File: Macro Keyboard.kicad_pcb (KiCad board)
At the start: 2 copper layers, 113 parts, among them J2901 FPC 1x24, Q2901 Q_PJFET_GDS, SW1001 KH-PS1611-54, SW1101 KH-PS1611-54, SW1201 KH-PS1611-54, SW1301 KH-PS1611-54, SW1401 KH-PS1611-54, SW1501 KH-PS1611-54, SW2801 SWITCH TACTILE SPST-NO 50MA 1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, SW601 KH-PS1611-54, SW701 KH-PS1611-54, SW801 KH-PS1611-54, SW901 KH-PS1611-54, U2701 PCA9745BTWJ, U2801 Pico-JER, U301 VEML7700, U401 PI4ULS5V201TAEX

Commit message: Checkpoint
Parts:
- C1701, C1801, C1901, C2001, C2101, C2201, C2301, C2401, C2501, C2601: moved to B.Cu
- moved C1701 25.3 mm to (26.5, 65.3), turned to 270 degrees
- moved D1701 22.2 mm to (26.4, 65.5), turned to 180 degrees
- moved C601 16.2 mm to (22.6, 46.6), turned to 270 degrees
- moved R602 14.7 mm to (29.0, 46.6), turned to 270 degrees
- moved R601 14.2 mm to (25.9, 46.6), turned to 90 degrees
- moved C2201 7.00 mm to (189.6, 65.3), turned to 90 degrees
- moved C1901 7.00 mm to (192.6, 28.4), turned to 90 degrees
- moved C2101 7.00 mm to (233.6, 64.4), turned to 90 degrees
- moved C2301 7.00 mm to (140.4, 67.0), turned to 90 degrees
- moved C2401 7.00 mm to (140.0, 101.2), turned to 90 degrees
- moved C2501 7.00 mm to (187.6, 101.4), turned to 90 degrees
- moved C1801 7.00 mm to (140.6, 28.1), turned to 90 degrees
- moved C2001 7.00 mm to (235.0, 26.7), turned to 90 degrees
- moved C2601 7.00 mm to (232.3, 101.8), turned to 90 degrees
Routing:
- net GND: track 0.00 -> 4.70 mm, vias 0 -> 1
- net +5V: track 0.00 -> 4.35 mm, vias 0 -> 1
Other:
- net class 1-wire added: clearance 0.4, trace_width 0.2, via_dia 0.8, via_drill 0.4
- net class Diff Pair added: clearance 0.2, trace_width 0.8125, via_dia 0.8, via_drill 0.4
- net class Power added: clearance 0.2, trace_width 0.5, via_dia 0.8, via_drill 0.4

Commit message: Switch NeoPixel to SK6812MINI-E
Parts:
- D1701, D1801, D1901, D2001, D2101, D2201, D2301, D2401, D2501, D2601: value WS2812B -> SK6812MINI-E; footprint LED_SMD:LED_WS2812B_PLCC4_5.0x5.0mm_P3.2mm -> Macro Keyboard:MX_SK6812MINI-E
- moved D2401 218.5 mm to (358.6, 104.6)
- moved D2601 216.3 mm to (443.5, 54.2)
- moved D2501 214.4 mm to (401.0, 79.4)
- moved D2201 211.6 mm to (401.0, 54.2)
- moved D2301 186.5 mm to (316.1, 129.8)
- moved D1801 182.8 mm to (316.1, 79.4)
- moved D1901 167.9 mm to (358.6, 54.2)
- moved D2101 125.8 mm to (358.6, 79.4)
- moved D2001 112.4 mm to (316.1, 104.6)
- moved D1701 6.90 mm to (26.4, 58.6), turned to 0 degrees
- moved C1701 6.33 mm to (20.4, 63.7), turned to 90 degrees
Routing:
- net GND: track 4.70 -> 0.00 mm, vias 1 -> 0
- net +5V: track 4.35 -> 0.00 mm, vias 1 -> 0
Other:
- board outline added: 3.6 x 3.3 mm

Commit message: design checkpoint
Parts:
- added C3001: 1 uF 10% 10V, Capacitor_SMD:C_0805_2012Metric_Pad1.18x1.45mm_HandSolder, F.Cu at (126.2, 92.7)
- added C3002: 1 uF 10% 10V, Capacitor_SMD:C_0805_2012Metric_Pad1.18x1.45mm_HandSolder, F.Cu at (126.2, 95.7)
- added C3003: 1 uF 10% 10V, Capacitor_SMD:C_0805_2012Metric_Pad1.18x1.45mm_HandSolder, F.Cu at (131.0, 92.7)
- added R3001: 4.7k 5%, Resistor_SMD:R_0805_2012Metric_Pad1.20x1.40mm_HandSolder, F.Cu at (126.2, 98.7)
- added R3002: 47k 5%, Resistor_SMD:R_0805_2012Metric_Pad1.20x1.40mm_HandSolder, F.Cu at (131.0, 95.7)
- added R3003: 4.7k 5%, Resistor_SMD:R_0805_2012Metric_Pad1.20x1.40mm_HandSolder, F.Cu at (135.8, 92.7)
- added R3004: 47k 5%, Resistor_SMD:R_0805_2012Metric_Pad1.20x1.40mm_HandSolder, F.Cu at (126.2, 101.6)
- added R3005: 150 5%, Resistor_SMD:R_0805_2012Metric_Pad1.20x1.40mm_HandSolder, F.Cu at (130.9, 98.7)
- added R3006: 2.7k 5%, Resistor_SMD:R_0805_2012Metric_Pad1.20x1.40mm_HandSolder, F.Cu at (135.7, 95.7)
- added R3007: 4.7k 5%, Resistor_SMD:R_0805_2012Metric_Pad1.20x1.40mm_HandSolder, F.Cu at (126.2, 104.6)
- added R3008: 68 5%, Resistor_SMD:R_0805_2012Metric_Pad1.20x1.40mm_HandSolder, F.Cu at (130.9, 101.6)
- added R3009: 68 5%, Resistor_SMD:R_0805_2012Metric_Pad1.20x1.40mm_HandSolder, F.Cu at (135.7, 98.6)
- added S3001: ENCODER-RGB-SWITCH, Macro Keyboard:ENCODER_LED_3, F.Cu at (117.0, 99.0)
- C2901, C2902, C2903, C2904, C2905, C2906, C2907, C2908, C2909, D2901, D2902, D2903, L2901, Q2901, R2901, R2902, U2801: moved to B.Cu
- moved C901 159.9 mm to (95.2, 81.6)
- moved R901 159.9 mm to (95.1, 84.6)
- moved R902 159.9 mm to (99.9, 81.6)
- moved C1001 152.2 mm to (96.5, 102.1)
- moved R1001 152.2 mm to (96.5, 105.0)
- moved R1002 152.2 mm to (101.3, 102.0)
- moved C1501 148.8 mm to (96.6, 120.7)
- moved R1501 148.8 mm to (96.6, 123.6)
- moved R1502 148.8 mm to (101.4, 120.6)
- moved C2001 147.1 mm to (96.4, 75.8)
- moved SW901 143.1 mm to (98.0, 80.0)
- moved C2601 140.6 mm to (92.2, 112.6)
- moved C2101 140.4 mm to (96.3, 93.7)
- moved SW1001 137.3 mm to (98.0, 99.0)
- moved SW1501 135.2 mm to (98.0, 118.0)
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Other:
- board size 3.6 x 3.3 mm -> 90.3 x 113.3 mm

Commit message: Starting routing
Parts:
- added DS**: e-paper_E2154FS091, Macro Keyboard:e-paper_E2154FS091, F.Cu at (55.4, 33.8)
- added REF**: MountingHole_M3_StandoffSMD, TMPPCB_R2:MountingHole_M3_StandoffSMD, F.Cu at (143.5, 35.5)
- added REF**: MountingHole_M3_StandoffSMD, TMPPCB_R2:MountingHole_M3_StandoffSMD, F.Cu at (56.4, 36.2)
- C1001, C1101, C1201, C1301, C1401, C1501, C2801, C2802, C701, C801, C901, R1001, R1002, R1101, R1102, R1201, R1202, R1301, R1302, R1401, R1402, R1501, R1502, R2801, R701, R702, R801, R802, R901, R902, SW2801: moved to B.Cu
- D2101, D2201, D2301: footprint Macro Keyboard:MX_SK6812MINI-E -> Macro Keyboard:MX_SK6812MINI-E_REV
- moved D2601 351.2 mm to (98.1, 118.1), turned to 180 degrees
- moved D2201 325.1 mm to (79.0, 99.0), turned to 180 degrees
- moved D2501 324.3 mm to (79.0, 118.1), turned to 180 degrees
- moved D2401 298.9 mm to (60.0, 118.1), turned to 180 degrees
- moved D1901 280.7 mm to (79.0, 80.0), turned to 180 degrees
- moved D2101 261.2 mm to (98.1, 99.0), turned to 180 degrees
- moved D2301 257.9 mm to (60.0, 99.0), turned to 180 degrees
- moved D1801 256.1 mm to (60.0, 80.0), turned to 180 degrees
- moved D2001 219.4 mm to (98.1, 80.0), turned to 180 degrees
- moved U2801 134.8 mm to (78.8, 57.7), turned to 270 degrees
- moved R2701 112.8 mm to (130.0, 57.3)
- moved R2702 112.8 mm to (134.8, 51.4)
- moved R2703 112.8 mm to (130.0, 54.4)
- moved R2704 112.8 mm to (134.8, 54.4)
- moved R2705 112.8 mm to (130.0, 60.3)
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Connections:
- J2901 pad 1: (no net) -> Net-(J2901-Pad1)
- J2901 pad 19: (no net) -> Net-(J2901-Pad19)
- J2901 pad 4: (no net) -> Net-(J2901-Pad4)
- J2901 pad 6: (no net) -> Net-(J2901-Pad6)
- J2901 pad 7: (no net) -> Net-(J2901-Pad7)
- R3005 pad 1: (no net) -> /Rotary Encoder 2/REnc_LED_R_5V
- R3008 pad 1: (no net) -> /Rotary Encoder 2/REnc_LED_G_5V
- R3009 pad 1: (no net) -> /Rotary Encoder 2/REnc_LED_B_5V
- U2701 pad 11: (no net) -> Net-(U2701-Pad11)
- U2701 pad 12: (no net) -> Net-(U2701-Pad12)
- U2701 pad 13: (no net) -> Net-(U2701-Pad13)
- U2701 pad 14: (no net) -> Net-(U2701-Pad14)
- U2701 pad 15: (no net) -> Net-(U2701-Pad15)
- U2701 pad 16: (no net) -> Net-(U2701-Pad16)
- U2701 pad 17: (no net) -> Net-(U2701-Pad17)
- U2701 pad 18: (no net) -> Net-(U2701-Pad18)
- U2701 pad 20: (no net) -> Net-(U2701-Pad20)
- U2701 pad 21: (no net) -> Net-(U2701-Pad21)
- U2701 pad 22: (no net) -> Net-(U2701-Pad22)
- U2701 pad 23: (no net) -> Net-(U2701-Pad23)
- U2701 pad 9: (no net) -> Net-(U2701-Pad9)
- U2801 pad 31: (no net) -> /Pico/GPIO_26_ADC0
- U2801 pad 32: (no net) -> /Pico/GPIO_27_ADC1
- U2801 pad 34: (no net) -> /Pico/GPIO_28_ADC2
- U2801 pad 37: (no net) -> Net-(U2801-Pad37)
- U2801 pad 39: (no net) -> Net-(U2801-Pad39)
- U2801 pad 41: (no net) -> Net-(U2801-Pad41)
- U2801 pad 43: (no net) -> Net-(U2801-Pad43)
- U2801 pad 44: (no net) -> Net-(U2801-Pad44)
- U2801 pad 45: (no net) -> Net-(U2801-Pad45)
- U2801 pad 46: (no net) -> Net-(U2801-Pad46)
- U2801 pad 47: (no net) -> Net-(U2801-Pad47)
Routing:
- net /Pico/GPIO_07: track 0.00 -> 74.0 mm, vias 0 -> 2
- net /Pico/GPIO_04: track 0.00 -> 45.8 mm, vias 0 -> 2
- net /Pico/GPIO_02: track 0.00 -> 38.7 mm, vias 0 -> 2
- net /Pico/GPIO_03: track 0.00 -> 38.6 mm, vias 0 -> 2
- net /LED 10/Neo LED 05/D_IN: track 0.00 -> 26.1 mm
- net /LED 10/Neo LED 08/D_IN: track 0.00 -> 21.7 mm
- net +5V: track 0.00 -> 20.0 mm
- net /LED 10/Neo LED 04/D_IN: track 0.00 -> 14.5 mm
- net /LED 10/Neo LED 09/D_IN: track 0.00 -> 14.5 mm
- net /LED 10/Neo LED 07/D_IN: track 0.00 -> 14.5 mm
- net /LED 10/Neo LED 06/D_IN: track 0.00 -> 14.5 mm
- net /LED 10/Neo LED 03/D_IN: track 0.00 -> 14.5 mm
- net /10 Group Switch/Switch 5/SW_RDIV: track 0.00 -> 8.77 mm
- net /10 Group Switch/Switch 4/SW_RDIV: track 0.00 -> 8.77 mm
- net /10 Group Switch/Switch 10/SW_RDIV: track 0.00 -> 8.77 mm
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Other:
- board size 90.3 x 113.3 mm -> 101.6 x 123.4 mm

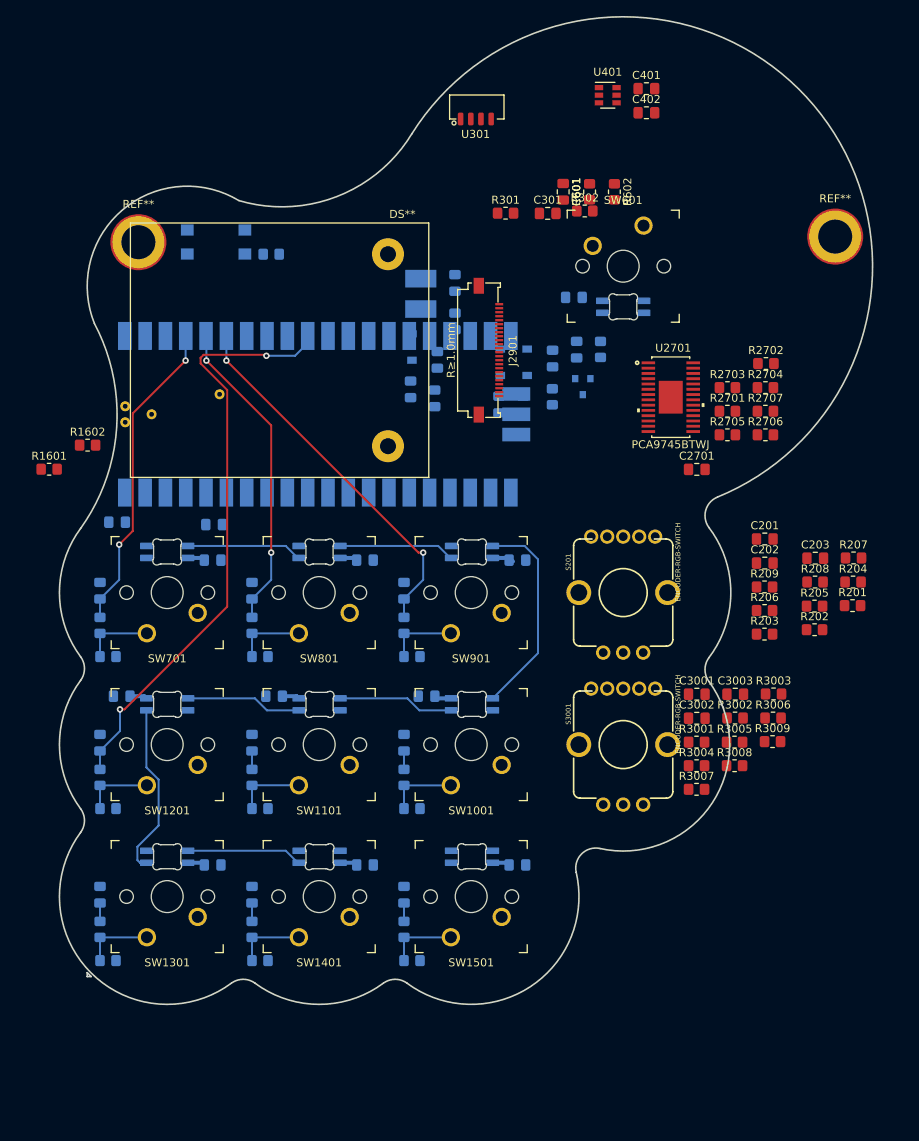
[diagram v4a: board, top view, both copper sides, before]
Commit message: Layout completed. Design check passes.
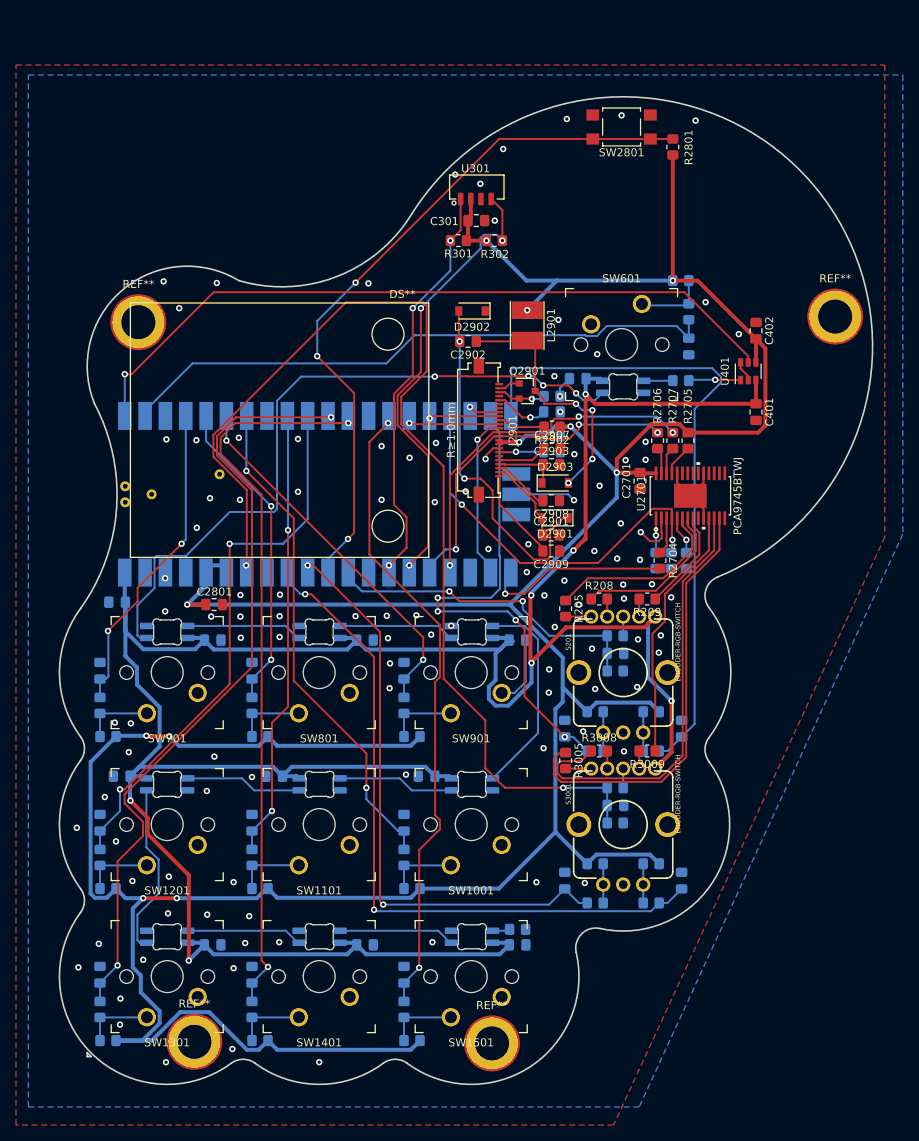
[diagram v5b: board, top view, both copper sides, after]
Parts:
- removed the REF** at (143.5, 35.5)
- removed the REF** at (56.4, 36.2)
- added REF**: MountingHole_M3_StandoffSMD, TMPPCB_R2:MountingHole_M3_StandoffSMD, F.Cu at (100.6, 136.3)
- added REF**: MountingHole_M3_StandoffSMD, TMPPCB_R2:MountingHole_M3_StandoffSMD, F.Cu at (63.4, 136.2)
- added REF**: MountingHole_M3_StandoffSMD, TMPPCB_R2:MountingHole_M3_StandoffSMD, F.Cu at (143.5, 45.5)
- added REF**: MountingHole_M3_StandoffSMD, TMPPCB_R2:MountingHole_M3_StandoffSMD, F.Cu at (56.4, 46.2)
- C201, C202, C203, C3001, C3002, C3003, C601, R1601, R1602, R201, R202, R203, R204, R206, R207, R2701, R2702, R2703, R3001, R3002, R3003, R3004, R3006, R3007, R601, R602: moved to B.Cu
- C2801, C2901, C2902, C2903, C2907, C2908, C2909, D2901, D2902, D2903, L2901, Q2901, R2801, R2902, SW2801: moved to F.Cu
- moved R1602 81.0 mm to (103.8, 122.1), turned to 180 degrees
- moved R1601 79.7 mm to (124.2, 53.5)
- moved SW2801 52.7 mm to (116.8, 21.8), turned to 180 degrees
- moved R2801 52.0 mm to (123.2, 24.3), turned to 90 degrees
- moved C401 42.7 mm to (133.6, 57.4), turned to 270 degrees
- moved U401 38.7 mm to (132.6, 52.3), turned to 90 degrees
- moved R201 36.9 mm to (113.5, 99.8)
- moved C201 34.4 mm to (109.7, 97.0), turned to 90 degrees
- moved R207 33.0 mm to (116.0, 89.8), turned to 180 degrees
- moved R205 31.1 mm to (109.8, 82.0), turned to 270 degrees
- moved C402 30.5 mm to (133.6, 47.3), turned to 270 degrees
- moved R3003 30.3 mm to (120.5, 118.8), turned to 180 degrees
- moved R204 30.0 mm to (120.5, 94.9)
- moved R202 29.3 mm to (113.5, 94.9), turned to 180 degrees
- moved C3001 28.6 mm to (109.7, 116.0), turned to 90 degrees
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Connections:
- net /RGB Driver/DRIVER_LED_B_5V renamed /RGB Driver/DRIVER_LED_SW1_B_5V
- net /RGB Driver/DRIVER_LED_G_5V renamed /RGB Driver/DRIVER_LED_SW1_G_5V
- net /RGB Driver/DRIVER_LED_R_5V renamed /RGB Driver/DRIVER_LED_SW1_R_5V
- net Net-(C2901-Pad1) renamed /eInk Display/DS_VGL
- net Net-(C2902-Pad1) renamed /eInk Display/DS_MOSFET_S
- net Net-(C2903-Pad1) renamed /eInk Display/DS_VGH
- net Net-(C2905-Pad2) renamed /eInk Display/DS_VDHR
- net Net-(C2906-Pad2) renamed /eInk Display/DS_VDDD
- net Net-(C2907-Pad1) renamed /eInk Display/DS_VSH
- net Net-(C2908-Pad2) renamed /eInk Display/DS_VSL
- net Net-(C2909-Pad2) renamed /eInk Display/DS_VCOM
- net Net-(J2901-Pad10) renamed /eInk Display/DS_BS1
- net Net-(J2901-Pad2) renamed /eInk Display/DS_GDR
- net Net-(J2901-Pad3) renamed /eInk Display/DS_MOSFET_D
- net Net-(R201-Pad2) renamed /Rotary Encoder 1/RE_SW_A
- net Net-(R203-Pad2) renamed /Rotary Encoder 1/RE_SW_B
- net Net-(R205-Pad2) renamed /Rotary Encoder 1/RES_DR
- net Net-(R206-Pad2) renamed /Rotary Encoder 1/RE_SW_RES
- net Net-(R208-Pad2) renamed /Rotary Encoder 1/RES_DG
- net Net-(R209-Pad2) renamed /Rotary Encoder 1/RES_DB
- net Net-(R3001-Pad2) renamed /Rotary Encoder 2/RE_SW_A
- net Net-(R3003-Pad2) renamed /Rotary Encoder 2/RE_SW_B
- net Net-(R3005-Pad2) renamed /Rotary Encoder 2/RES_DR
- net Net-(R3006-Pad2) renamed /Rotary Encoder 2/RE_SW_RES
- net Net-(R3008-Pad2) renamed /Rotary Encoder 2/RES_DG
- net Net-(R3009-Pad2) renamed /Rotary Encoder 2/RES_DB
- C3001 pad 1: /Rotary Encoder 2/REnc_A -> /Pico/GPIO_26_ADC0
- C3002 pad 2: /Rotary Encoder 2/REnc_B -> /Pico/GPIO_27_ADC1
- C3003 pad 2: /Rotary Encoder 2/REnc_SW -> /Pico/GPIO_28_ADC2
- R3001 pad 1: /Rotary Encoder 2/REnc_A -> /Pico/GPIO_26_ADC0
- R3003 pad 1: /Rotary Encoder 2/REnc_B -> /Pico/GPIO_27_ADC1
- R3005 pad 1: /Rotary Encoder 2/REnc_LED_R_5V -> /RGB Driver/DRIVER_LED_SW2_B_5V
- R3006 pad 1: /Rotary Encoder 2/REnc_SW -> /Pico/GPIO_28_ADC2
- R3007 pad 2: /Rotary Encoder 2/REnc_SW -> /Pico/GPIO_28_ADC2
- R3008 pad 1: /Rotary Encoder 2/REnc_LED_G_5V -> /RGB Driver/DRIVER_LED_SW2_G_5V
- R3009 pad 1: /Rotary Encoder 2/REnc_LED_B_5V -> /RGB Driver/DRIVER_LED_SW2_R_5V
- U2701 pad 11: Net-(U2701-Pad11) -> /RGB Driver/DRIVER_LED_SW2_R_5V
- U2701 pad 12: Net-(U2701-Pad12) -> /RGB Driver/DRIVER_LED_SW2_G_5V
- U2701 pad 13: Net-(U2701-Pad13) -> /RGB Driver/DRIVER_LED_SW2_B_5V
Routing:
- net +3V3: track 0.00 -> 455.2 mm, vias 0 -> 11
- net +5V: track 20.0 -> 336.2 mm, vias 0 -> 7
- net /Pico/GPIO_28_ADC2: track 0.00 -> 135.9 mm, vias 0 -> 2
- net /Pico/GPIO_08: track 2.30 -> 97.5 mm, vias 0 -> 2
- net /Level Converter/D_IN_3V3: track 0.00 -> 92.4 mm, vias 0 -> 1
- net /Pico/GPIO_09: track 2.30 -> 90.5 mm, vias 0 -> 2
- net /Pico/GPIO_27_ADC1: track 0.00 -> 88.0 mm, vias 0 -> 2
- net /LED 10/Neo LED 02/D_IN: track 0.00 -> 87.9 mm, vias 0 -> 4
- net Net-(R2801-Pad2): track 0.00 -> 87.7 mm, vias 0 -> 3
- net /Pico/GPIO_15: track 0.00 -> 84.1 mm
- net /Pico/GPIO_10: track 2.30 -> 79.3 mm, vias 0 -> 2
- net /Pico/GPIO_01: track 0.00 -> 76.8 mm
- net /Pico/GPIO_26_ADC0: track 0.00 -> 73.8 mm, vias 0 -> 2
- net /Pico/GPIO_14: track 0.00 -> 62.2 mm, vias 0 -> 4
- net /Pico/GPIO_05: track 2.30 -> 61.9 mm, vias 0 -> 2
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- added copper zone on B.Cu, net GND
- added copper zone on F.Cu, net GND
